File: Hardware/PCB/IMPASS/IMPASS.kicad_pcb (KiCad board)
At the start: 2 copper layers, 73.9 x 100 mm, 159 parts, among them J1 POWER, J11 SOLENOIDES, J17 PUENTE H_1, J18 PUENTE H_2, J19 SOLENOIDES, J2 POWER, J20 SENSORES, J21 PROG, J22 VM, J23 EJE1, J24 EJE2, J25 EJE3, J26 SOLENOIDES, J27 PUENTE H, J28 PUENTE H, J29 SENSORES, Q10 DMN3008SFG, Q11 DMN3008SFG, Q12 DMN3008SFG, Q13 DMN3008SFG, Q14 DMN3008SFG, Q15 DMN3008SFG, Q16 DMN3008SFG, Q17 DMN3008SFG, Q18 DMN3008SFG, Q19 DMN3008SFG, Q20 DMN3008SFG, Q21 DMN3008SFG, Q22 DMN3008SFG, Q23 DMN3008SFG, Q24 DMN3008SFG, Q43 DMN3008SFG, Q44 DMN3008SFG, Q45 DMN3008SFG, Q49 2N7002, Q50 2N7002, Q51 2N7002, Q52 2N7002, Q53 2N7002, Q54 2N7002, Q55 2N7002, Q56 2N7002, Q57 2N7002, Q58 2N7002, Q59 2N7002, Q60 2N7002, Q61 2N7002, Q62 2N7002, Q63 2N7002, Q64 2N7002, Q65 2N7002, Q66 2N7002, Q67 2N7002, Q68 2N7002, Q69 2N7002, Q70 DMN3008SFG, Q71 DMN3008SFG, Q72 DMN3008SFG, Q73 DMN3008SFG, Q74 DMN3008SFG, Q75 DMN3008SFG, Q76 DMN3008SFG, Q77 DMN3008SFG, Q9 DMN3008SFG, SW1 RESET, SW2 BOOT, U10 AMS1117-3.3, U11 AMS1117-5.0, U12 AS5047D, U13 MCP3008, U14 ESP32-S3-WROOM-1, U2 LM75B, U3 ACS712xLCTR-30A, U4 ACS712xLCTR-30A, U5 ACS712xLCTR-30A, U6 ACS712xLCTR-30A, U7 ACS712xLCTR-30A, U8 ACS712xLCTR-30A, U9 LM75B

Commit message: Hardware: update schematic and PCB layout
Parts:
- removed Q70, Q72, Q74, Q76: DMN3008SFG, Package_SON:Diodes_PowerDI3333-8
- added Q1: BC847BDW1, Package_TO_SOT_SMD:SOT-363_SC-70-6, F.Cu at (156.9, 45.4)
- added Q2: DMP3013SFV, Package_SON:Diodes_PowerDI3333-8, F.Cu at (154.5, 41.3)
- added Q25: DMP3013SFV, Package_SON:Diodes_PowerDI3333-8, F.Cu at (159.5, 68.0)
- added Q26: DMP3013SFV, Package_SON:Diodes_PowerDI3333-8, F.Cu at (159.5, 72.0)
- added Q3: DMP3013SFV, Package_SON:Diodes_PowerDI3333-8, F.Cu at (154.5, 37.0)
- added Q4: DMP3013SFV, Package_SON:Diodes_PowerDI3333-8, F.Cu at (143.0, 41.3)
- added Q5: BC847BDW1, Package_TO_SOT_SMD:SOT-363_SC-70-6, F.Cu at (145.5, 45.4)
- added Q6: DMP3013SFV, Package_SON:Diodes_PowerDI3333-8, F.Cu at (143.0, 37.1)
- added Q7: BC847BDW1, Package_TO_SOT_SMD:SOT-363_SC-70-6, F.Cu at (134.8, 45.4)
- added Q8: DMP3013SFV, Package_SON:Diodes_PowerDI3333-8, F.Cu at (132.2, 41.4)
- added R59: 10k, Resistor_SMD:R_0603_1608Metric, F.Cu at (153.7, 46.5)
- added R60: 10k, Resistor_SMD:R_0603_1608Metric, F.Cu at (160.2, 45.0)
- added R61: 10k, Resistor_SMD:R_0603_1608Metric, F.Cu at (160.2, 46.5)
- added R62: 10k, Resistor_SMD:R_0603_1608Metric, F.Cu at (153.7, 45.0)
- added R63: 10k, Resistor_SMD:R_0603_1608Metric, F.Cu at (148.8, 46.5)
- added R64: 10k, Resistor_SMD:R_0603_1608Metric, F.Cu at (142.2, 46.5)
- added R65: 10k, Resistor_SMD:R_0603_1608Metric, F.Cu at (148.8, 45.0)
- added R66: 10k, Resistor_SMD:R_0603_1608Metric, F.Cu at (142.2, 45.0)
- added R67: 10k, Resistor_SMD:R_0603_1608Metric, F.Cu at (138.0, 46.5)
- added R68: 10k, Resistor_SMD:R_0603_1608Metric, F.Cu at (131.5, 46.5)
- added R69: 10k, Resistor_SMD:R_0603_1608Metric, F.Cu at (138.0, 45.0)
- added R70: 10k, Resistor_SMD:R_0603_1608Metric, F.Cu at (131.5, 45.0)
- added R71: 10k, Resistor_SMD:R_0603_1608Metric, F.Cu at (138.7, 64.6)
- added R72: 10k, Resistor_SMD:R_0603_1608Metric, F.Cu at (132.0, 64.5)
- added R73: 10k, Resistor_SMD:R_0603_1608Metric, F.Cu at (138.7, 63.0)
- added R74: 10k, Resistor_SMD:R_0603_1608Metric, F.Cu at (132.0, 63.0)
- added R75: 10k, Resistor_SMD:R_0603_1608Metric, F.Cu at (150.7, 64.7)
- added R76: 10k, Resistor_SMD:R_0603_1608Metric, F.Cu at (143.0, 64.6)
- added R77: 10k, Resistor_SMD:R_0603_1608Metric, F.Cu at (150.7, 63.1)
- added R78: 10k, Resistor_SMD:R_0603_1608Metric, F.Cu at (143.0, 63.1)
- added R79: 10k, Resistor_SMD:R_0603_1608Metric, F.Cu at (162.0, 64.5)
- added R80: 10k, Resistor_SMD:R_0603_1608Metric, F.Cu at (154.7, 64.4)
- added R81: 10k, Resistor_SMD:R_0603_1608Metric, F.Cu at (162.0, 63.0)
- added R82: 10k, Resistor_SMD:R_0603_1608Metric, F.Cu at (154.7, 62.9)
- Q10, Q17, Q22: value DMN3008SFG -> BC847BDW1; footprint Package_SON:Diodes_PowerDI3333-8 -> Package_TO_SOT_SMD:SOT-363_SC-70-6
- Q13, Q14, Q18, Q21, Q9: value DMN3008SFG -> DMP3013SFV
- moved Q10 23.5 mm to (135.3, 64.0)
- moved Q21 9.51 mm to (148.9, 72.0), turned to 180 degrees
- moved Q17 8.83 mm to (147.2, 64.0), turned to 180 degrees
- moved C24 6.38 mm to (131.8, 56.7), turned to 90 degrees
- moved U5 6.23 mm to (130.0, 51.9), turned to 0 degrees
- moved U8 5.69 mm to (161.2, 58.4), turned to 180 degrees
- moved C13 5.62 mm to (132.1, 48.2), turned to 0 degrees
- moved U4 5.61 mm to (142.0, 52.0), turned to 0 degrees
- moved C15 5.49 mm to (159.5, 52.8), turned to -90 degrees
- moved U3 5.37 mm to (154.5, 52.0), turned to 0 degrees
- moved Q11 4.98 mm to (137.0, 41.4)
- moved Q23 4.98 mm to (155.0, 68.0), turned to 180 degrees
- moved Q71 4.85 mm to (159.4, 41.4)
- moved Q73 4.80 mm to (148.1, 41.3)
- moved Q13 4.79 mm to (137.9, 67.9), turned to 180 degrees
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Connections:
- J23 pad 2: /Placa_potencia/Eje1/OUT1_1 -> /Placa_potencia/Sensores_potencia/OUT1_2
- J23 pad 4: /Placa_potencia/Eje1/OUT2_1 -> /Placa_potencia/Sensores_potencia/OUT2_2
- J24 pad 2: /Placa_potencia/Eje2/OUT3_1 -> /Placa_potencia/Sensores_potencia/OUT3_2
- J24 pad 4: /Placa_potencia/Eje2/OUT4_1 -> /Placa_potencia/Sensores_potencia/OUT4_2
- J25 pad 2: /Placa_potencia/Eje3/OUT6_1 -> /Placa_potencia/Sensores_potencia/OUT6_2
- J25 pad 4: /Placa_potencia/Eje3/OUT5_1 -> /Placa_potencia/Sensores_potencia/OUT5_2
- J29 pad 7: /Placa_potencia/Sensores_potencia/SCL -> /Placa_potencia/Sensores_potencia/SDA
- J29 pad 8: /Placa_potencia/Sensores_potencia/SDA -> /Placa_potencia/Sensores_potencia/SCL
- Q10 pad 1: /Placa_potencia/Eje2/OUT3_2 -> GND1
- Q10 pad 2: /Placa_potencia/Eje2/OUT3_2 -> Net-(Q10A-B1)
- Q10 pad 3: /Placa_potencia/Eje2/OUT3_2 -> Net-(Q10B-C2)
- Q10 pad 4: /Placa_potencia/Eje2/~PWM3 -> GND1
- Q10 pad 5: 12v -> Net-(Q10B-B2)
- Q13 pad 1: /Placa_potencia/Eje2/OUT4_1 -> 12v
- Q13 pad 2: /Placa_potencia/Eje2/OUT4_1 -> 12v
- Q13 pad 3: /Placa_potencia/Eje2/OUT4_1 -> 12v
- Q13 pad 4: /Placa_potencia/Eje2/PWM4 -> Net-(Q10A-C1)
- Q13 pad 5: 12v -> /Placa_potencia/Eje2/OUT4_1
- Q14 pad 1: /Placa_potencia/Eje2/OUT4_2 -> 12v
- Q14 pad 2: /Placa_potencia/Eje2/OUT4_2 -> 12v
- Q14 pad 3: /Placa_potencia/Eje2/OUT4_2 -> 12v
- Q14 pad 4: /Placa_potencia/Eje2/~PWM4 -> Net-(Q10B-C2)
- Q14 pad 5: 12v -> /Placa_potencia/Eje2/OUT4_2
- Q17 pad 1: /Placa_potencia/Eje3/OUT5_1 -> GND1
- Q17 pad 2: /Placa_potencia/Eje3/OUT5_1 -> Net-(Q17A-B1)
- Q17 pad 3: /Placa_potencia/Eje3/OUT5_1 -> Net-(Q17B-C2)
- Q17 pad 4: /Placa_potencia/Eje3/PWM5 -> GND1
- Q17 pad 5: 12v -> Net-(Q17B-B2)
- Q18 pad 1: /Placa_potencia/Eje3/OUT5_2 -> 12v
- Q18 pad 2: /Placa_potencia/Eje3/OUT5_2 -> 12v
- Q18 pad 3: /Placa_potencia/Eje3/OUT5_2 -> 12v
- Q18 pad 4: /Placa_potencia/Eje3/~PWM5 -> Net-(Q17A-C1)
- Q18 pad 5: 12v -> /Placa_potencia/Eje3/OUT5_1
- Q21 pad 1: /Placa_potencia/Eje3/OUT6_1 -> 12v
- Q21 pad 2: /Placa_potencia/Eje3/OUT6_1 -> 12v
- Q21 pad 3: /Placa_potencia/Eje3/OUT6_1 -> 12v
- Q21 pad 4: /Placa_potencia/Eje3/PWM6 -> Net-(Q17B-C2)
- Q21 pad 5: 12v -> /Placa_potencia/Eje3/OUT5_2
- Q22 pad 1: /Placa_potencia/Eje3/OUT6_2 -> GND1
- Q22 pad 2: /Placa_potencia/Eje3/OUT6_2 -> Net-(Q22A-B1)
- Q22 pad 3: /Placa_potencia/Eje3/OUT6_2 -> Net-(Q22B-C2)
- Q22 pad 4: /Placa_potencia/Eje3/~PWM6 -> GND1
- Q22 pad 5: 12v -> Net-(Q22B-B2)
- Q9 pad 1: /Placa_potencia/Eje2/OUT3_1 -> 12v
- Q9 pad 2: /Placa_potencia/Eje2/OUT3_1 -> 12v
- Q9 pad 3: /Placa_potencia/Eje2/OUT3_1 -> 12v
- Q9 pad 4: /Placa_potencia/Eje2/PWM3 -> Net-(Q7B-C2)
- Q9 pad 5: 12v -> /Placa_potencia/Eje2/OUT3_2
- U3 pad 3: /Placa_potencia/Eje1/OUT1_2 -> /Placa_potencia/Sensores_potencia/OUT1_2
- U3 pad 4: /Placa_potencia/Eje1/OUT1_2 -> /Placa_potencia/Sensores_potencia/OUT1_2
- U4 pad 3: /Placa_potencia/Eje1/OUT2_2 -> /Placa_potencia/Sensores_potencia/OUT2_2
- U4 pad 4: /Placa_potencia/Eje1/OUT2_2 -> /Placa_potencia/Sensores_potencia/OUT2_2
- U5 pad 3: /Placa_potencia/Eje2/OUT3_2 -> /Placa_potencia/Sensores_potencia/OUT3_2
- U5 pad 4: /Placa_potencia/Eje2/OUT3_2 -> /Placa_potencia/Sensores_potencia/OUT3_2
- U6 pad 3: /Placa_potencia/Eje2/OUT4_2 -> /Placa_potencia/Sensores_potencia/OUT4_2
- U6 pad 4: /Placa_potencia/Eje2/OUT4_2 -> /Placa_potencia/Sensores_potencia/OUT4_2
- U7 pad 3: /Placa_potencia/Eje3/OUT5_2 -> /Placa_potencia/Sensores_potencia/OUT5_2
- U7 pad 4: /Placa_potencia/Eje3/OUT5_2 -> /Placa_potencia/Sensores_potencia/OUT5_2
- U8 pad 3: /Placa_potencia/Eje3/OUT6_2 -> /Placa_potencia/Sensores_potencia/OUT6_2
- U8 pad 4: /Placa_potencia/Eje3/OUT6_2 -> /Placa_potencia/Sensores_potencia/OUT6_2
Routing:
- net 12v: track 160.7 -> 243.7 mm, vias 9 -> 4
- net /Placa_potencia/Sensores_potencia/SCL: track 46.1 -> 118.1 mm
- net GND1: track 353.2 -> 420.8 mm, vias 4 -> 18
- net /Placa_potencia/Sensores_potencia/OUT6_2: track 0.00 -> 57.6 mm, vias 0 -> 1
- net /Placa_potencia/Sensores_potencia/OUT1_2: track 0.00 -> 46.6 mm, vias 0 -> 2
- net /Placa_potencia/Sensores_potencia/SDA: track 48.6 -> 89.1 mm
- net /Placa_potencia/Sensores_potencia/OUT2_2: track 0.00 -> 39.9 mm, vias 0 -> 1
- net /Placa_potencia/Sensores_potencia/OUT5_2: track 0.00 -> 37.7 mm, vias 0 -> 2
- net /Placa_potencia/Eje1/OUT1_1: track 57.6 -> 22.1 mm, vias 3 -> 4
- net /Placa_potencia/Eje1/OUT2_1: track 54.3 -> 20.3 mm, vias 2 -> 4
- net /Placa_potencia/Eje3/OUT6_1: track 57.3 -> 24.3 mm
- net /Placa_potencia/Sensores_potencia/OUT4_2: track 0.00 -> 30.2 mm, vias 0 -> 1
- net /Placa_potencia/Eje2/OUT3_1: track 48.1 -> 21.0 mm, vias 3 -> 4
- net /Placa_potencia/Eje3/OUT5_1: track 42.0 -> 19.0 mm
- net /Placa_potencia/Eje3/~PWM5: track 7.64 -> 28.6 mm, vias 1 -> 2
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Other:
- board text removed: "PCB potencia IMPASS"

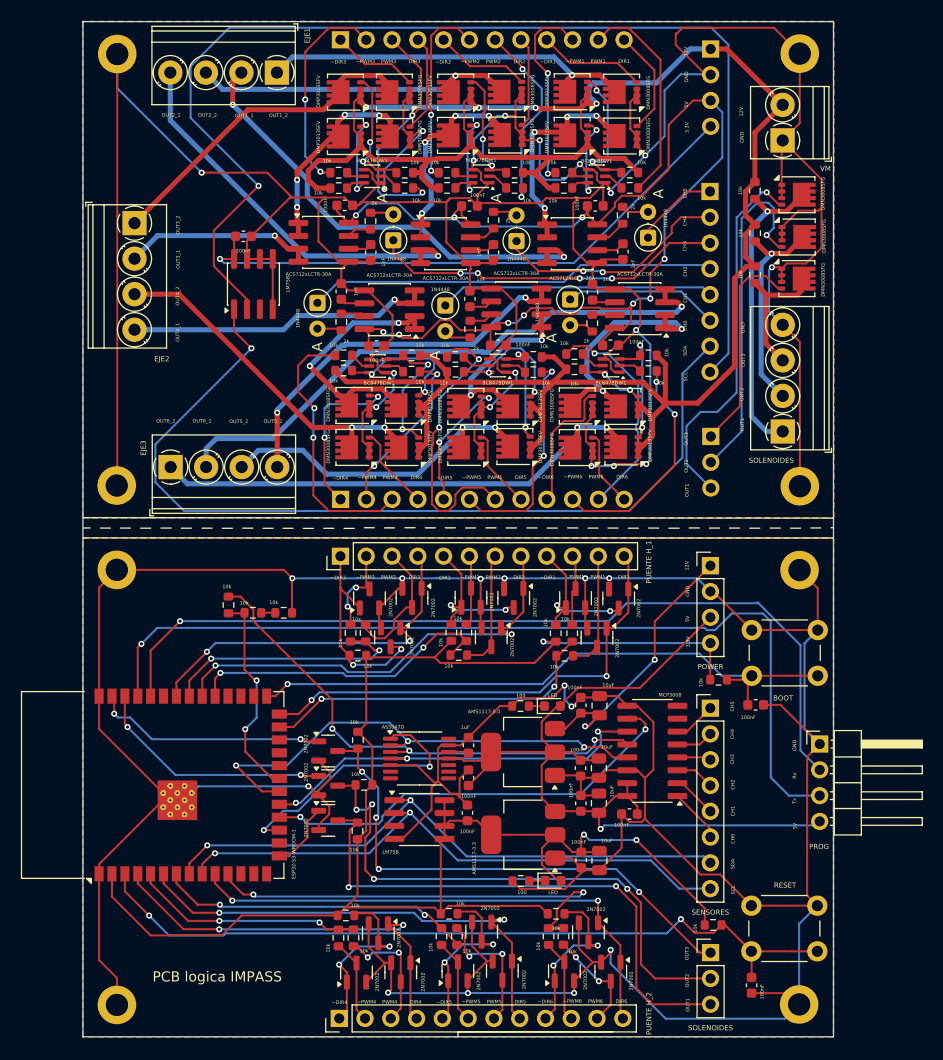
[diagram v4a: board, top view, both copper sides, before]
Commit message: Hardware: update schematic and PCB layout 	- Replace the LDOs with buck converters 	- Replace AD5047D with LIS3DH
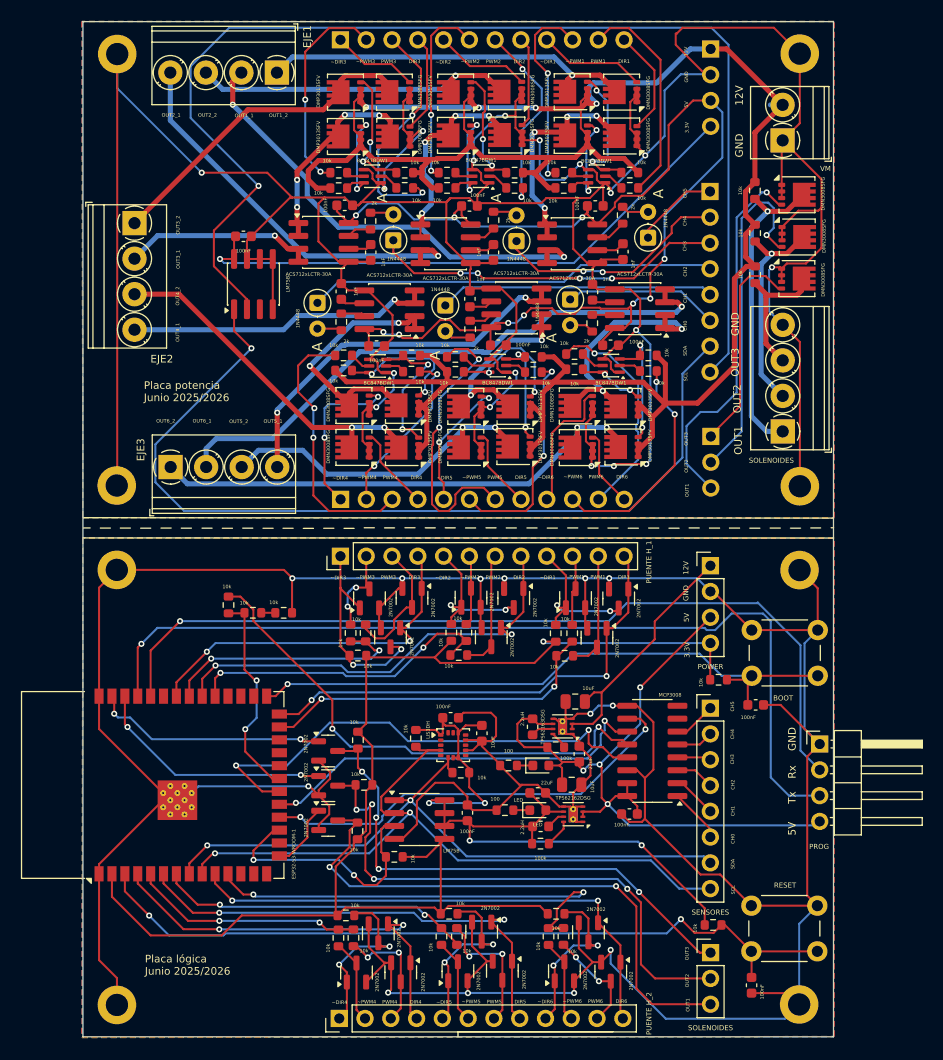
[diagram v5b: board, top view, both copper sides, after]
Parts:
- removed C10, C9: 100nF, Capacitor_SMD:C_0603_1608Metric
- removed C18: 1uF, Capacitor_SMD:C_0603_1608Metric
- removed C3, C8: 10uF, Capacitor_SMD:C_0805_2012Metric
- removed D7: LED, LED_SMD:LED_0603_1608Metric
- removed R33: 100, Resistor_SMD:R_0603_1608Metric
- removed U11: AMS1117-5.0, Package_TO_SOT_SMD:SOT-223-3_TabPin2
- removed U12: AS5047D, Package_SO:TSSOP-14_4.4x5mm_P0.65mm
- added C28: 10uF, Capacitor_SMD:C_0603_1608Metric, F.Cu at (145.6, 100.2)
- added D9: LED, LED_SMD:LED_0603_1608Metric, F.Cu at (151.1, 107.8)
- added L1: 2.2uH, Inductor_SMD:L_0603_1608Metric, F.Cu at (150.6, 99.6)
- added L2: 2.2uH, Inductor_SMD:L_0603_1608Metric, F.Cu at (151.4, 109.4)
- added R83: 100k, Resistor_SMD:R_0603_1608Metric, F.Cu at (152.9, 101.6)
- added R84: 100k, Resistor_SMD:R_0603_1608Metric, F.Cu at (151.4, 111.1)
- added R85: 100, Resistor_SMD:R_0603_1608Metric, F.Cu at (147.9, 107.8)
- added R86: 10k, Resistor_SMD:R_0603_1608Metric, F.Cu at (137.0, 112.4)
- added R87: 10k, Resistor_SMD:R_0603_1608Metric, F.Cu at (143.5, 104.1)
- added R88: 10k, Resistor_SMD:R_0603_1608Metric, F.Cu at (139.1, 100.7)
- added U1: TPS62162DSG, Package_SON:WSON-8-1EP_2x2mm_P0.5mm_EP0.9x1.6mm_ThermalVias, F.Cu at (154.6, 108.2)
- added U15: TPS62163DSG, Package_SON:WSON-8-1EP_2x2mm_P0.5mm_EP0.9x1.6mm_ThermalVias, F.Cu at (153.6, 99.5)
- C5: value 100nF -> 10uF; footprint Capacitor_SMD:C_0603_1608Metric -> Capacitor_SMD:C_0805_2012Metric
- C6: value 100nF -> 22uF
- C7: value 10uF -> 22uF; footprint Capacitor_SMD:C_0805_2012Metric -> Capacitor_SMD:C_0603_1608Metric
- U10: value AMS1117-3.3 -> LIS3DH; footprint Package_TO_SOT_SMD:SOT-223-3_TabPin2 -> Package_LGA:LGA-16_3x3mm_P0.5mm_LayoutBorder3x5y
- moved U10 11.2 mm to (142.8, 101.4), turned to 0 degrees
- moved C7 9.02 mm to (151.1, 106.1), turned to 0 degrees
- moved C19 6.16 mm to (142.5, 98.7), turned to 0 degrees
- moved R34 5.98 mm to (148.2, 103.4)
- moved D8 5.97 mm to (151.4, 103.4)
- moved C6 4.81 mm to (155.2, 102.3)
- moved C4 2.42 mm to (154.8, 97.1), turned to 180 degrees
- moved C5 2.04 mm to (154.4, 105.3), turned to 0 degrees
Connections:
- C19 pad 1: +5V -> +3.3V
- C6 pad 1: /12v -> +5V
- U10 pad 1: GND -> +3.3V
- U10 pad 2: +3.3V -> unconnected-(U10-NC-Pad2)
- U10 pad 3: +5V -> unconnected-(U10-NC-Pad3)
- U14 pad 17: cs_INC -> OS_1
- U9 pad 3: unconnected-(U9-O.S.-Pad3) -> OS_1
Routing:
- net +3.3V: track 172.8 -> 208.2 mm, vias 3 -> 5
- net cs_INC: track 26.6 -> 0.00 mm, vias 2 -> 0
- net OS_1: track 0.00 -> 24.9 mm, vias 0 -> 2
- net GND: track 413.3 -> 399.8 mm
- net +5V: track 86.1 -> 73.1 mm, vias 1 -> 4
- net /Placa_logica/SCL: track 57.8 -> 70.9 mm
- net /Placa_logica/SDA: track 59.1 -> 66.5 mm
- net /12v: track 28.1 -> 24.9 mm, vias 2 -> 0
- net Net-(U1-PG): track 0.00 -> 2.75 mm
- net Net-(U15-SW): track 0.00 -> 2.24 mm
- net Net-(U12-VDD3V3): track 2.01 -> 0.00 mm
- net Net-(U1-SW): track 0.00 -> 1.87 mm
- net Net-(U15-PG): track 0.00 -> 1.76 mm
- net Net-(D9-K): track 0.00 -> 1.62 mm
- net Net-(D7-K): track 1.58 -> 0.00 mm
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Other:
- board text added: "Placa lógica Junio 2025/2026"
- board text added: "Placa potencia Junio 2025/2026"
- board text removed: "PCB logica IMPASS"
